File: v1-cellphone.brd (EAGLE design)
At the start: 103.1 x 46.7 mm, 93 parts, among them J1 AVRISP, J2 ZX62D-B-5P8, J4 FTDI, J5 BATTERY INPUT, Q1 MIC, Q2 NTR4501N-D, Q3 NTR4501N-D, U1 MCP73831, U2 MEGA1284, U3 GSM_UC15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

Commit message: Final for release. Passes ERC, DRC.
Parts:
- removed C20: 33pF 16V, rcl_custom:0603-B
- removed C22: 100uF 16V, rcl_custom:C1210K
- removed JP2: (no value), SparkFun-Connectors:1X04_LOCK
- added J6: (no value), SparkFun-Connectors:1X04_LOCK
- moved LED5 13.4 mm to (51.8, 5.21), turned to 0 degrees
- moved R9 11.8 mm to (51.8, 8.64), turned to 90 degrees
- moved C26 2.67 mm to (50.8, 31.1)
- moved C9 1.78 mm to (1.78, 16.9)
- moved R3 1.78 mm to (1.78, 10.5)
- moved TP13 1.78 mm to (4.83, 12.4)
- moved TP9 1.78 mm to (1.78, 13.7)
- moved X3 1.78 mm to (20.2, 11.0)
- moved TP7 1.78 mm to (35.7, 12.4)
- moved TP6 1.78 mm to (35.7, 15.0)
- moved TP8 1.78 mm to (35.7, 9.91)
- moved C8 1.52 mm to (63.2, 39.8)
- moved L1 1.52 mm to (61.3, 39.8)
- moved L2 1.17 mm to (62.6, 42.4)
- moved TP3 1.02 mm to (53.1, 19.3)
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- renumbered JP1 to J3, JP3 to J7
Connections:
- removed net PC0: U2.19
- removed net PC1: U2.20
- removed net PC2: U2.21
- removed net PC3: U2.22
- removed net PC4: U2.23
- removed net PC5: U2.24
- removed net PC6: U2.25
- removed net PC7: U2.26
- net GND: no longer C20.2, C22.2
- net PA4: now also J6.1; no longer JP2.1
- net PA5: now also J6.2; no longer JP2.2
- net PA6: now also J6.3; no longer JP2.3
- net PA7: now also J6.4; no longer JP2.4
- net VBAT: no longer C20.1, C22.1
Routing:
- net NETLIGHT: track 4.19 -> 16.7 mm
- net AGND: track 28.9 -> 23.7 mm
- net VDD_EXT: track 42.2 -> 46.8 mm
- net SIM_RSTR: track 10.7 -> 9.08 mm
- net SIM_CLKR: track 12.3 -> 10.7 mm
- net PA4: track 4.36 -> 5.71 mm
- net PA5: track 7.13 -> 8.48 mm
- net PA6: track 10.1 -> 11.5 mm
- net PA7: track 12.9 -> 14.2 mm
- net ANT: track 5.95 -> 7.00 mm
- net SPK1P: track 9.14 -> 9.90 mm
- net N$23: track 10.1 -> 9.36 mm
- net SIM_VDD: track 56.2 -> 55.5 mm
- net VBAT: track 35.2 -> 35.9 mm
- net UC15STATUS: track 10.7 -> 11.3 mm
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
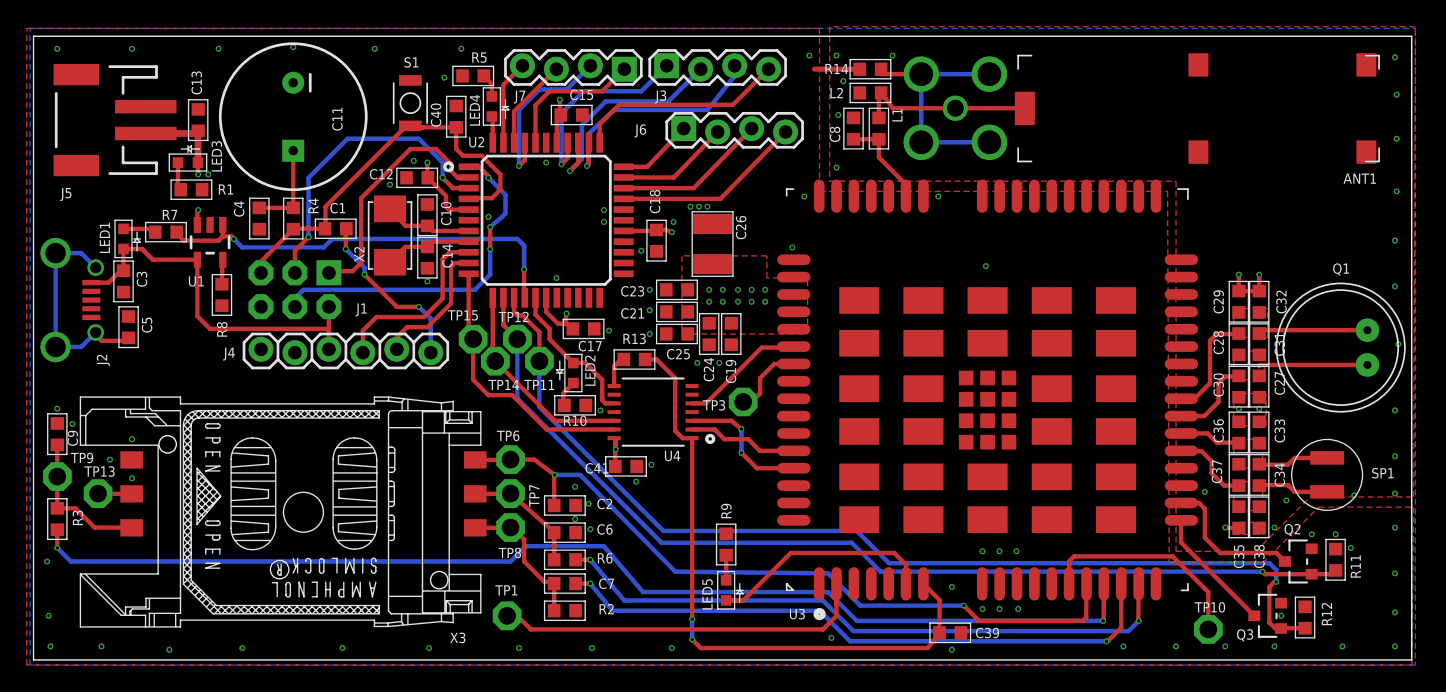
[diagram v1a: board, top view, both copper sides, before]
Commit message: Fixed switched R2 and C7 silkscreen labels.
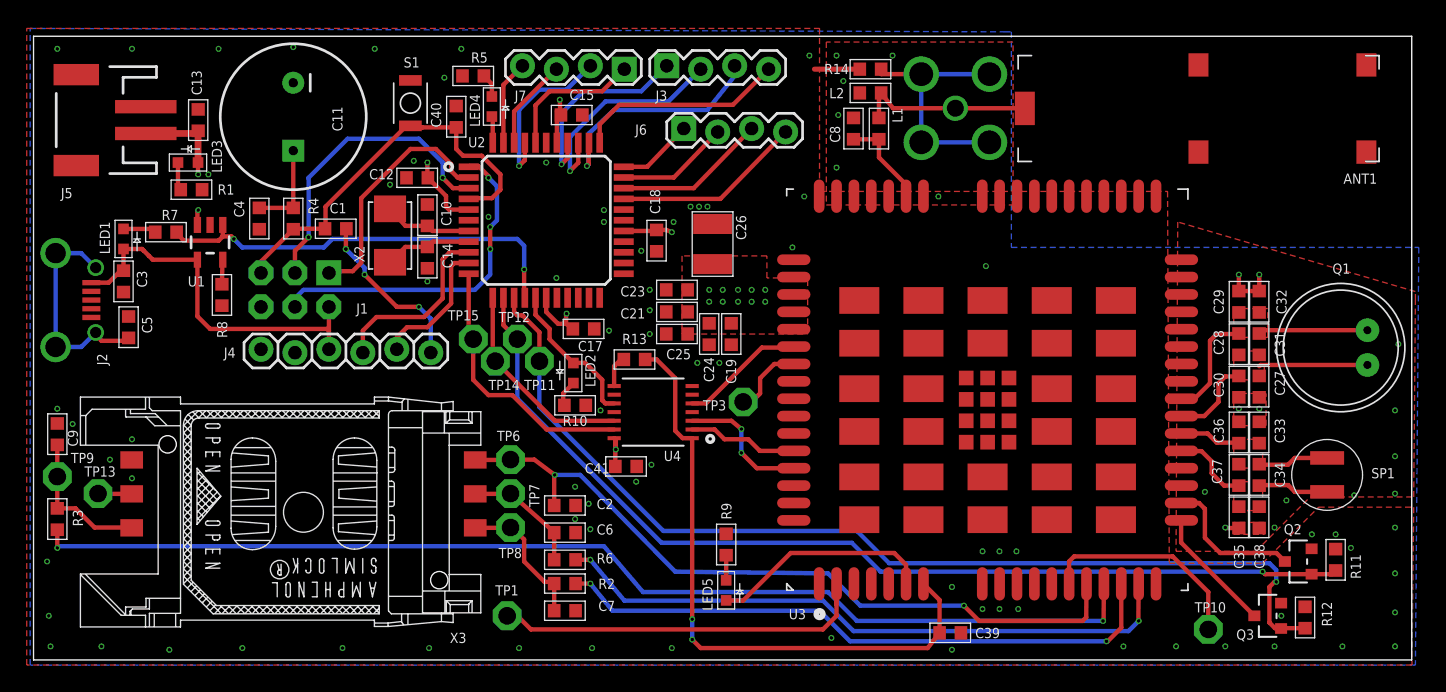
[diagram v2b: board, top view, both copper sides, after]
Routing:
- net N$1: track 85.8 -> 84.9 mm
- net MOSI: track 26.2 -> 25.6 mm
- net AGND: vias 24 -> 18
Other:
- board text added: "3G Module Prototype Board v1 Wickerbox Electronics http://wickerbox.net/"
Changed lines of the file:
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@@
 <layer number="49" name="Reference" color="7" fill="1" visible="no" active="yes"/>
 <layer number="50" name="dxf" color="12" fill="1" visible="no" active="no"/>
-<layer number="51" name="tDocu" color="7" fill="1" visible="no" active="yes"/>
+<layer number="51" name="tDocu" color="7" fill="1" visible="yes" active="yes"/>
 <layer number="52" name="bDocu" color="7" fill="1" visible="yes" active="yes"/>
 <layer number="53" name="tGND_GNDA" color="7" fill="1" visible="no" active="no"/>
@@
 <wire x1="103.104" y1="46.66" x2="0" y2="46.66" width="0" layer="20"/>
 <wire x1="0" y1="46.66" x2="0" y2="0" width="0" layer="20"/>
+<text x="3.302" y="2.921" size="1.016" layer="26" font="vector" ratio="15" rot="MR0" align="bottom-right">3G Module Prototype Board v1
+Wickerbox Electronics
+http://wickerbox.net/</text>
 </plain>
 <attributes>
@@
 </element>
 <element name="R2" library="rcl_custom" package="0603-B" value="22" x="39.751" y="5.715" smashed="yes" rot="R180">
-<attribute name="NAME" x="42.253" y="3.413" size="0.762" layer="25" font="vector" ratio="15"/>
+<attribute name="NAME" x="42.253" y="5.318" size="0.762" layer="25" font="vector" ratio="15"/>
 <attribute name="VALUE" x="40.551" y="7.765" size="1" layer="27" ratio="10" rot="R180"/>
 </element>
@@
 </element>
 <element name="C7" library="rcl_custom" package="0603-B" value="33pF 16V" x="39.751" y="3.683" smashed="yes">
-<attribute name="NAME" x="42.253" y="5.318" size="0.762" layer="25" font="vector" ratio="15"/>
+<attribute name="NAME" x="42.253" y="3.667" size="0.762" layer="25" font="vector" ratio="15"/>
 <attribute name="VALUE" x="38.951" y="1.633" size="1" layer="27" ratio="10"/>
 </element>
@@
 <vertex x="-0.254" y="-0.381"/>
 <vertex x="-0.254" y="47.244"/>
-<vertex x="103.378" y="47.244"/>
+<vertex x="72.644" y="46.99"/>
+<vertex x="73.152" y="46.99"/>
+<vertex x="73.152" y="30.861"/>
+<vertex x="103.632" y="30.861"/>
 <vertex x="103.378" y="-0.381"/>
 </polygon>
@@
 <wire x1="33.274" y1="36.957" x2="32.618" y2="36.957" width="0.3302" layer="1"/>
 <wire x1="32.618" y1="36.957" x2="32.554" y2="36.893" width="0.3302" layer="1"/>
-<wire x1="34.036" y1="36.068" x2="35.306" y2="34.798" width="0.3302" layer="16"/>
-<wire x1="35.306" y1="34.798" x2="35.306" y2="33.401" width="0.3302" layer="16"/>
-<wire x1="35.306" y1="33.401" x2="35.052" y2="33.147" width="0.3302" layer="16"/>
-<wire x1="35.052" y1="33.147" x2="34.163" y2="32.385" width="0.3302" layer="16"/>
 <via x="34.163" y="32.385" extent="1-16" drill="0.254" diameter="0.4572"/>
 <wire x1="34.163" y1="32.385" x2="34.163" y2="30.734" width="0.3302" layer="1"/>
 <via x="34.163" y="30.734" extent="1-16" drill="0.254" diameter="0.4572"/>
 <wire x1="34.163" y1="30.734" x2="34.163" y2="28.829" width="0.3302" layer="16"/>
+<wire x1="34.163" y1="32.385" x2="34.671" y2="32.893" width="0.3302" layer="16"/>
+<wire x1="34.671" y1="32.893" x2="34.671" y2="35.433" width="0.3302" layer="16"/>
+<wire x1="34.671" y1="35.433" x2="34.036" y2="36.068" width="0.3302" layer="16"/>
 </signal>
 <signal name="!RESET">
@@
 <wire x1="40.754" y1="37.198" x2="40.132" y2="36.576" width="0.3302" layer="1"/>
 <via x="40.132" y="36.576" extent="1-16" drill="0.254" diameter="0.4572"/>
-<wire x1="40.132" y1="36.576" x2="41.021" y2="37.465" width="0.3302" layer="16"/>
-<wire x1="41.021" y1="37.465" x2="41.021" y2="40.005" width="0.3302" layer="16"/>
-<wire x1="41.021" y1="40.005" x2="42.799" y2="41.783" width="0.3302" layer="16"/>
+<wire x1="40.132" y1="39.116" x2="42.799" y2="41.783" width="0.3302" layer="16"/>
 <wire x1="42.799" y1="41.783" x2="47.498" y2="41.783" width="0.3302" layer="16"/>
 <wire x1="47.498" y1="41.783" x2="49.911" y2="44.196" width="0.3302" layer="16"/>
+<wire x1="40.132" y1="39.116" x2="40.132" y2="36.576" width="0.3302" layer="16"/>
 </signal>
 <signal name="PA2">
@@
 <vertex x="84.709" y="7.874"/>
 <vertex x="103.378" y="7.874"/>
-<vertex x="103.378" y="46.99"/>
+<vertex x="103.378" y="27.432"/>
+<vertex x="102.362" y="27.686"/>
+<vertex x="73.152" y="36.576"/>
+<vertex x="73.152" y="46.99"/>
 <vertex x="60.452" y="46.99"/>
 </polygon>
@@
 <wire x1="89.192" y1="9.868" x2="89.154" y2="9.906" width="0.3302" layer="1"/>
 <polygon width="0.381" layer="1" rank="5">
-<vertex x="59.563" y="47.371"/>
-<vertex x="59.563" y="35.814"/>
-<vertex x="85.471" y="35.814"/>
 <vertex x="85.471" y="8.128"/>
 <vertex x="91.44" y="8.128"/>
 <vertex x="95.504" y="12.192"/>
 <vertex x="103.251" y="12.192"/>
-<vertex x="103.378" y="47.371"/>
+<vertex x="103.378" y="26.924"/>
+<vertex x="103.378" y="27.559"/>
+<vertex x="85.598" y="32.766"/>
 </polygon>
 <via x="60.071" y="45.212" extent="1-16" drill="0.254" diameter="0.4572"/>
@@
 <via x="60.198" y="40.767" extent="1-16" drill="0.254" diameter="0.4572"/>
 <via x="64.262" y="45.212" extent="1-16" drill="0.254" diameter="0.4572"/>
-<via x="101.854" y="45.085" extent="1-16" drill="0.254" diameter="0.4572"/>
-<via x="101.981" y="42.291" extent="1-16" drill="0.254" diameter="0.4572"/>
-<via x="101.981" y="38.989" extent="1-16" drill="0.254" diameter="0.4572"/>
-<via x="101.981" y="35.052" extent="1-16" drill="0.254" diameter="0.4572"/>
-<via x="101.854" y="31.369" extent="1-16" drill="0.254" diameter="0.4572"/>
-<via x="101.854" y="27.94" extent="1-16" drill="0.254" diameter="0.4572"/>
 <via x="102.108" y="23.622" extent="1-16" drill="0.254" diameter="0.4572"/>
 <via x="101.854" y="18.669" extent="1-16" drill="0.254" diameter="0.4572"/>
@@
 <via x="98.806" y="12.319" extent="1-16" drill="0.254" diameter="0.4572"/>
 <via x="93.726" y="11.938" extent="1-16" drill="0.254" diameter="0.4572"/>
+<polygon width="0.3302" layer="1">
+<vertex x="59.309" y="46.228"/>
+<vertex x="59.309" y="34.036"/>
+<vertex x="73.279" y="34.036"/>
+<vertex x="73.279" y="46.228"/>
+</polygon>
 </signal>
 <signal name="N$1">
@@
 <wire x1="61.595" y1="2.921" x2="59.436" y2="5.08" width="0.3302" layer="16"/>
 <wire x1="59.436" y1="5.08" x2="45.593" y2="5.08" width="0.3302" layer="16"/>
-<wire x1="35.687" y1="7.366" x2="2.794" y2="7.366" width="0.3302" layer="16"/>
-<wire x1="2.794" y1="7.366" x2="1.778" y2="8.382" width="0.3302" layer="16"/>
 <via x="1.778" y="8.382" extent="1-16" drill="0.254" diameter="0.4572"/>
 <wire x1="1.778" y1="8.382" x2="1.778" y2="9.741" width="0.3302" layer="1"/>
 <wire x1="45.593" y1="5.08" x2="42.672" y2="8.509" width="0.3302" layer="16"/>
-<wire x1="42.672" y1="8.509" x2="36.83" y2="8.509" width="0.3302" layer="16"/>
-<wire x1="36.83" y1="8.509" x2="35.687" y2="7.366" width="0.3302" layer="16"/>
+<wire x1="42.672" y1="8.509" x2="1.905" y2="8.509" width="0.3302" layer="16"/>
+<wire x1="1.905" y1="8.509" x2="1.778" y2="8.382" width="0.3302" layer="16"/>
 </signal>
 <signal name="N$13">
@@
 </signal>
 </signals>
-<errors>
-</errors>
 </board>
 </drawing>
+<compatibility>
+<note version="6.3" minversion="6.2.2" severity="warning">
+Since Version 6.2.2 text objects can contain more than one line,
+which will not be processed correctly with this version.
+</note>
+</compatibility>
 </eagle>
